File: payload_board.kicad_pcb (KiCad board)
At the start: 4 copper layers, 100 x 100 mm, 92 parts, among them IC1 RP2040_QFN56, IC2 AZ1117CH-3.3TRG1, J1 Cam_PicoLock, J10 503398-1892, J12 FC Breakout, J15 SWC, J2 Cam_Conn, J3 Antenna_Conn, J4 usb jumper, J6 Breakout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

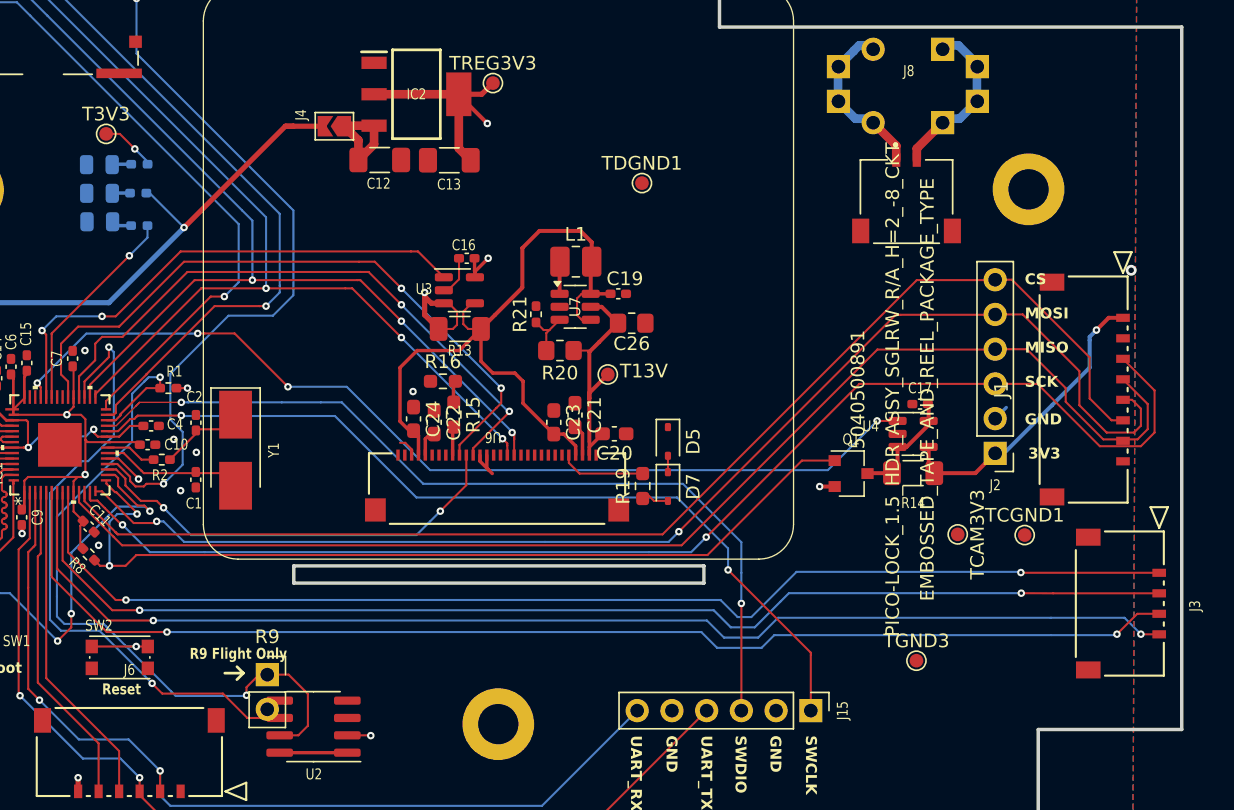
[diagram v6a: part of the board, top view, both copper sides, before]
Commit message: Update placement blocking connectors
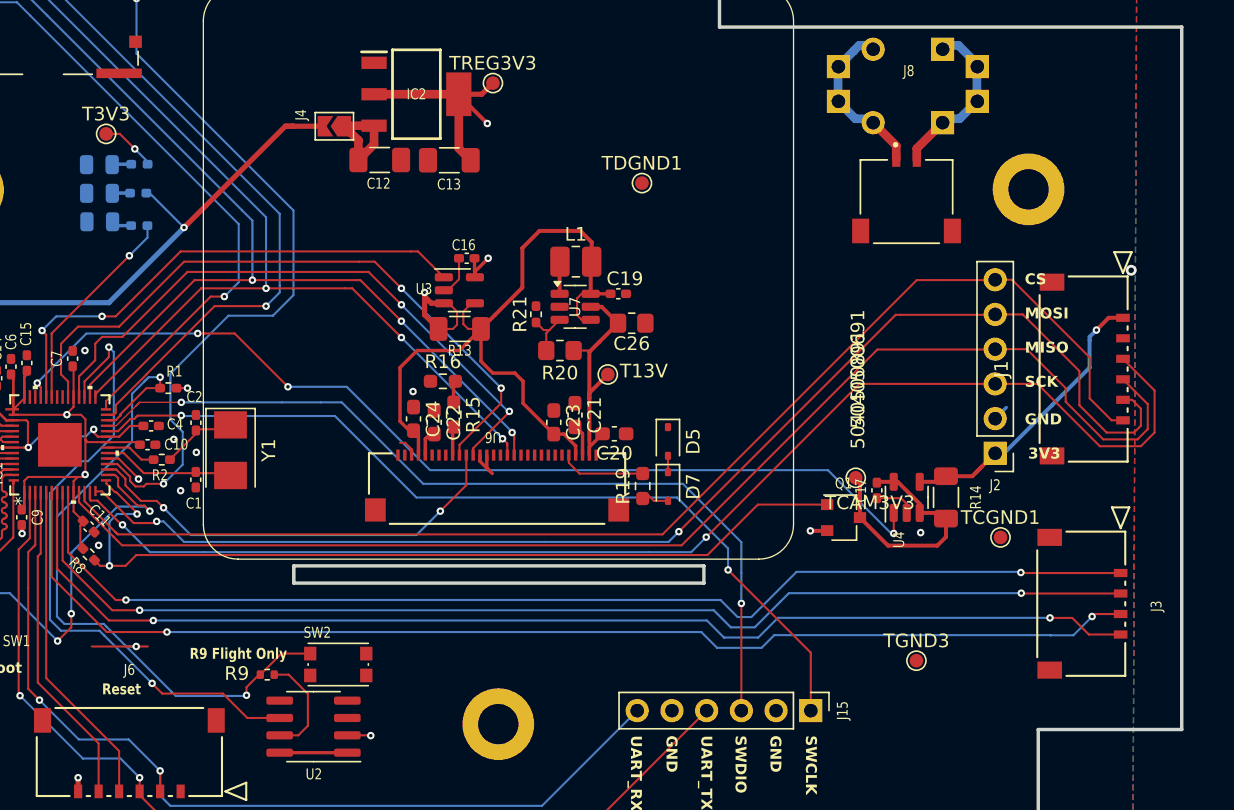
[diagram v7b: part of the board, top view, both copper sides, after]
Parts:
- J1: footprint PayloadBoard:Molex_Pico_CON_5040500891 -> PayloadBoard:Molex_Pico_CON_5040500691
- R9: footprint Connector_PinSocket_2.54mm:PinSocket_1x02_P2.54mm_Vertical -> Resistor_SMD:R_0402_1005Metric
- Y1: footprint Crystal:Crystal_SMD_5032-2Pin_5.0x3.2mm_HandSoldering -> Crystal:Crystal_SMD_5032-2Pin_5.0x3.2mm
- moved SW2 16.0 mm to (51.3, 97.7)
- moved TCAM3V3 8.53 mm to (89.1, 84.1)
- moved C17 7.06 mm to (90.7, 85.0), turned to 90 degrees
- moved U4 4.67 mm to (92.9, 85.5), turned to 90 degrees
- moved Q1 3.27 mm to (88.2, 87.0)
- moved R14 2.99 mm to (95.7, 85.5), turned to 90 degrees
- moved J3 2.82 mm to (108.5, 91.0)
- moved TCGND1 1.78 mm to (99.7, 88.4)
- moved Y1 0.37 mm to (43.4, 82.0)
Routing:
- net Cam_3.3v: track 8.38 -> 18.4 mm
- net /~{RESET}: track 50.3 -> 54.6 mm
- net GND: track 13.8 -> 16.8 mm, vias 12 -> 13
- net BURN_A: track 88.3 -> 85.4 mm
- net BURN_B: track 87.6 -> 84.7 mm
- net I2C1_SDA: track 90.5 -> 87.7 mm
- net I2C1_SCL: track 89.5 -> 86.7 mm
- net Cam_RST: track 66.5 -> 64.6 mm
- net ADC1: track 71.3 -> 73.0 mm

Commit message: Updated footprints to refelct part avaliability
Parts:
- C22, C23: value 1.0uF -> 1uF
- R19: footprint Resistor_SMD:R_0603_1608Metric_Pad0.98x0.95mm_HandSolder -> Resistor_SMD:R_0402_1005Metric
- R21: value 1k -> 1K
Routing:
- net GND: vias 13 -> 16
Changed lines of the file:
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@@
 			(drillshape 0)
 			(scaleselection 1)
-			(outputdirectory "Manufacturing/payload_board_rev073_gbr")
+			(outputdirectory "Manufacturing/payload_board_rev074_gbr")
 		)
 	)
@@
 	(net 88 "unconnected-(J10-DAT1-Pad8)")
 	(net 89 "Net-(U7-FB)")
-	(footprint "Resistor_SMD:R_0603_1608Metric_Pad0.98x0.95mm_HandSolder"
+	(footprint "Resistor_SMD:R_0402_1005Metric"
 		(layer "F.Cu")
 		(at 73.55 84.6625 90)
-		(descr "Resistor SMD 0603 (1608 Metric), square (rectangular) end terminal, IPC_7351 nominal with elongated pad for handsoldering. (Body size source: IPC-SM-782 page 72, https://www.pcb-3d.com/wordpress/wp-content/uploads/ipc-sm-782a_amendment_1_and_2.pdf), generated with kicad-footprint-generator")
-		(tags "resistor handsolder")
+		(descr "Resistor SMD 0402 (1005 Metric), square (rectangular) end terminal, IPC_7351 nominal, (Body size source: IPC-SM-782 page 72, https://www.pcb-3d.com/wordpress/wp-content/uploads/ipc-sm-782a_amendment_1_and_2.pdf), generated with kicad-footprint-generator")
+		(tags "resistor")
 		(property "Reference" "R19"
-			(at 0 -1.43 90)
+			(at 0 -1.17 90)
 			(layer "F.SilkS")
 			(effects
@@
 		)
 		(property "Value" "50"
-			(at 0 1.43 90)
+			(at 0 1.17 90)
 			(layer "F.Fab")
 			(effects
@@
 			)
 		)
-		(property "Footprint" "Resistor_SMD:R_0603_1608Metric_Pad0.98x0.95mm_HandSolder"
+		(property "Footprint" "Resistor_SMD:R_0402_1005Metric"
 			(at 0 0 90)
 			(unlocked yes)
@@
 		(attr smd)
 		(fp_line
-			(start -0.254724 -0.5225)
-			(end 0.254724 -0.5225)
+			(start -0.153641 -0.38)
+			(end 0.153641 -0.38)
 			(stroke
 				(width 0.12)
@@
 		)
 		(fp_line
-			(start -0.254724 0.5225)
-			(end 0.254724 0.5225)
+			(start -0.153641 0.38)
+			(end 0.153641 0.38)
 			(stroke
 				(width 0.12)
@@
 		)
 		(fp_line
-			(start 1.65 -0.73)
-			(end 1.65 0.73)
+			(start 0.93 -0.47)
+			(end 0.93 0.47)
 			(stroke
 				(width 0.05)
@@
 		)
 		(fp_line
-			(start -1.65 -0.73)
-			(end 1.65 -0.73)
+			(start -0.93 -0.47)
+			(end 0.93 -0.47)
 			(stroke
 				(width 0.05)
@@
 		)
 		(fp_line
-			(start 1.65 0.73)
-			(end -1.65 0.73)
+			(start 0.93 0.47)
+			(end -0.93 0.47)
 			(stroke
 				(width 0.05)
@@
 		)
 		(fp_line
-			(start -1.65 0.73)
-			(end -1.65 -0.73)
+			(start -0.93 0.47)
+			(end -0.93 -0.47)
 			(stroke
 				(width 0.05)
@@
 		)
 		(fp_line
-			(start 0.8 -0.4125)
-			(end 0.8 0.4125)
+			(start 0.525 -0.27)
+			(end 0.525 0.27)
 			(stroke
 				(width 0.1)
@@
 		)
 		(fp_line
-			(start -0.8 -0.4125)
-			(end 0.8 -0.4125)
+			(start -0.525 -0.27)
+			(end 0.525 -0.27)
 			(stroke
 				(width 0.1)
@@
 		)
 		(fp_line
-			(start 0.8 0.4125)
-			(end -0.8 0.4125)
+			(start 0.525 0.27)
+			(end -0.525 0.27)
 			(stroke
 				(width 0.1)
@@
 		)
 		(fp_line
-			(start -0.8 0.4125)
-			(end -0.8 -0.4125)
+			(start -0.525 0.27)
+			(end -0.525 -0.27)
 			(stroke
 				(width 0.1)
@@
 			(effects
 				(font
-					(size 0.4 0.4)
-					(thickness 0.06)
+					(size 0.26 0.26)
+					(thickness 0.04)
 				)
 			)
 		)
 		(pad "1" smd roundrect
-			(at -0.9125 0 90)
-			(size 0.975 0.95)
+			(at -0.51 0 90)
+			(size 0.54 0.64)
 			(layers "F.Cu" "F.Paste" "F.Mask")
 			(roundrect_rratio 0.25)
@@
 		)
 		(pad "2" smd roundrect
-			(at 0.9125 0 90)
-			(size 0.975 0.95)
+			(at 0.51 0 90)
+			(size 0.54 0.64)
 			(layers "F.Cu" "F.Paste" "F.Mask")
 			(roundrect_rratio 0.25)
@@
 			(pintype "passive")
 		)
-		(model "${KICAD8_3DMODEL_DIR}/Resistor_SMD.3dshapes/R_0603_1608Metric.wrl"
+		(model "${KICAD8_3DMODEL_DIR}/Resistor_SMD.3dshapes/R_0402_1005Metric.wrl"
 			(offset
 				(xyz 0 0 0)
@@
 		(tags "capacitor handsolder")
 		(property "Reference" "C23"
-			(at 0 -1.43 -90)
+			(at 0 -1.43 90)
 			(layer "F.SilkS")
 			(effects
@@
 			)
 		)
-		(property "Value" "1.0uF"
-			(at 0 1.43 -90)
+		(property "Value" "1uF"
+			(at 0 1.43 90)
 			(layer "F.Fab")
 			(effects
@@
 		)
 		(fp_text user "${REFERENCE}"
-			(at 0 0 -90)
+			(at 0 0 90)
 			(layer "F.Fab")
 			(effects
@@
 			)
 		)
-		(property "Value" "1k"
+		(property "Value" "1K"
 			(at 0 1.17 90)
 			(layer "F.Fab")
@@
 		(tags "SC-59")
 		(property "Reference" "Q1"
-			(at 0 -2.5 360)
+			(at 0 -2.5 0)
 			(layer "F.SilkS")
 			(effects
@@
 		)
 		(property "Value" "Q_PMOS_GSD"
-			(at 0 2.5 360)
+			(at 0 2.5 0)
 			(layer "F.Fab")
 			(effects
@@
 		)
 		(property "Footprint" ""
-			(at 0 0 360)
+			(at 0 0 0)
 			(layer "F.Fab")
 			(hide yes)
@@
 		)
 		(property "Datasheet" ""
-			(at 0 0 360)
+			(at 0 0 0)
 			(layer "F.Fab")
 			(hide yes)
@@
 		)
 		(property "Description" "P-MOSFET transistor, gate/source/drain"
-			(at 0 0 360)
+			(at 0 0 0)
 			(layer "F.Fab")
 			(hide yes)
@@
 		(tags "capacitor handsolder")
 		(property "Reference" "C22"
-			(at 0 -1.43 -90)
+			(at 0 -1.43 90)
 			(layer "F.SilkS")
 			(effects
@@
 			)
 		)
-		(property "Value" "1.0uF"
-			(at 0 1.43 -90)
+		(property "Value" "1uF"
+			(at 0 1.43 90)
 			(layer "F.Fab")
 			(effects
@@
 		)
 		(fp_text user "${REFERENCE}"
-			(at 0 0 -90)
+			(at 0 0 90)
 			(layer "F.Fab")
 			(effects
@@
 	)
 	(via
+		(at 94.75 73.35)
+		(size 0.55)
+		(drill 0.25)
+		(layers "F.Cu" "B.Cu")
+		(free yes)
+		(net 1)
+	)
+	(via
 		(at 28.15 88.14)
 		(size 0.55)
@@
 	)
 	(via
+		(at 94.54 75.83)
+		(size 0.55)
+		(drill 0.25)
+		(layers "F.Cu" "B.Cu")
+		(free yes)
+		(net 1)
+	)
+	(via
 		(at 32.75 74.75)
 		(size 0.55)
@@
 		(layers "F.Cu" "B.Cu")
 		(free yes)
+		(net 1)
+	)
+	(via
+		(at 95.17 70.71)
+		(size 0.55)
+		(drill 0.25)
+		(layers "F.Cu" "B.Cu")
+		(free yes)
